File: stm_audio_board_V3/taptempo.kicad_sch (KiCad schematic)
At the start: 2 parts

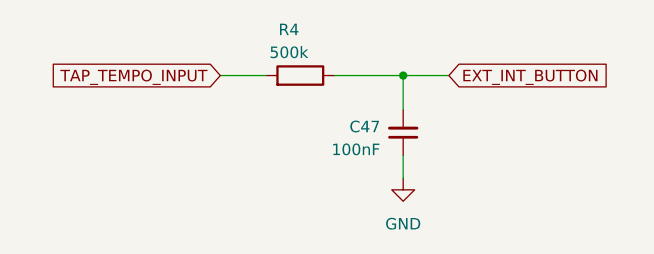
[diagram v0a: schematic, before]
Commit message: Input and output stages are made and assembly started on pcb view
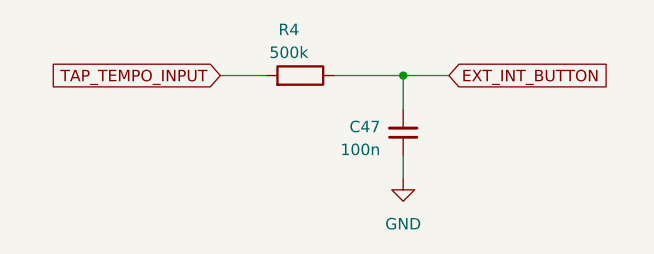
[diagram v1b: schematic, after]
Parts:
- C47: value 100nF -> 100n; footprint Capacitor_SMD:C_0603_1608Metric_Pad1.08x0.95mm_HandSolder -> Capacitor_SMD:C_0603_1608Metric
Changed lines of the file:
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@@
       (effects (font (size 1.27 1.27)) (justify right))
     )
-    (property "Value" "100nF" (at 54.61 53.9686 0)
+    (property "Value" "100n" (at 54.61 53.9686 0)
       (effects (font (size 1.27 1.27)) (justify right))
     )
-    (property "Footprint" "Capacitor_SMD:C_0603_1608Metric_Pad1.08x0.95mm_HandSolder" (at 57.15 52.07 0)
+    (property "Footprint" "Capacitor_SMD:C_0603_1608Metric" (at 57.15 52.07 0)
       (effects (font (size 1.27 1.27)) hide)
     )

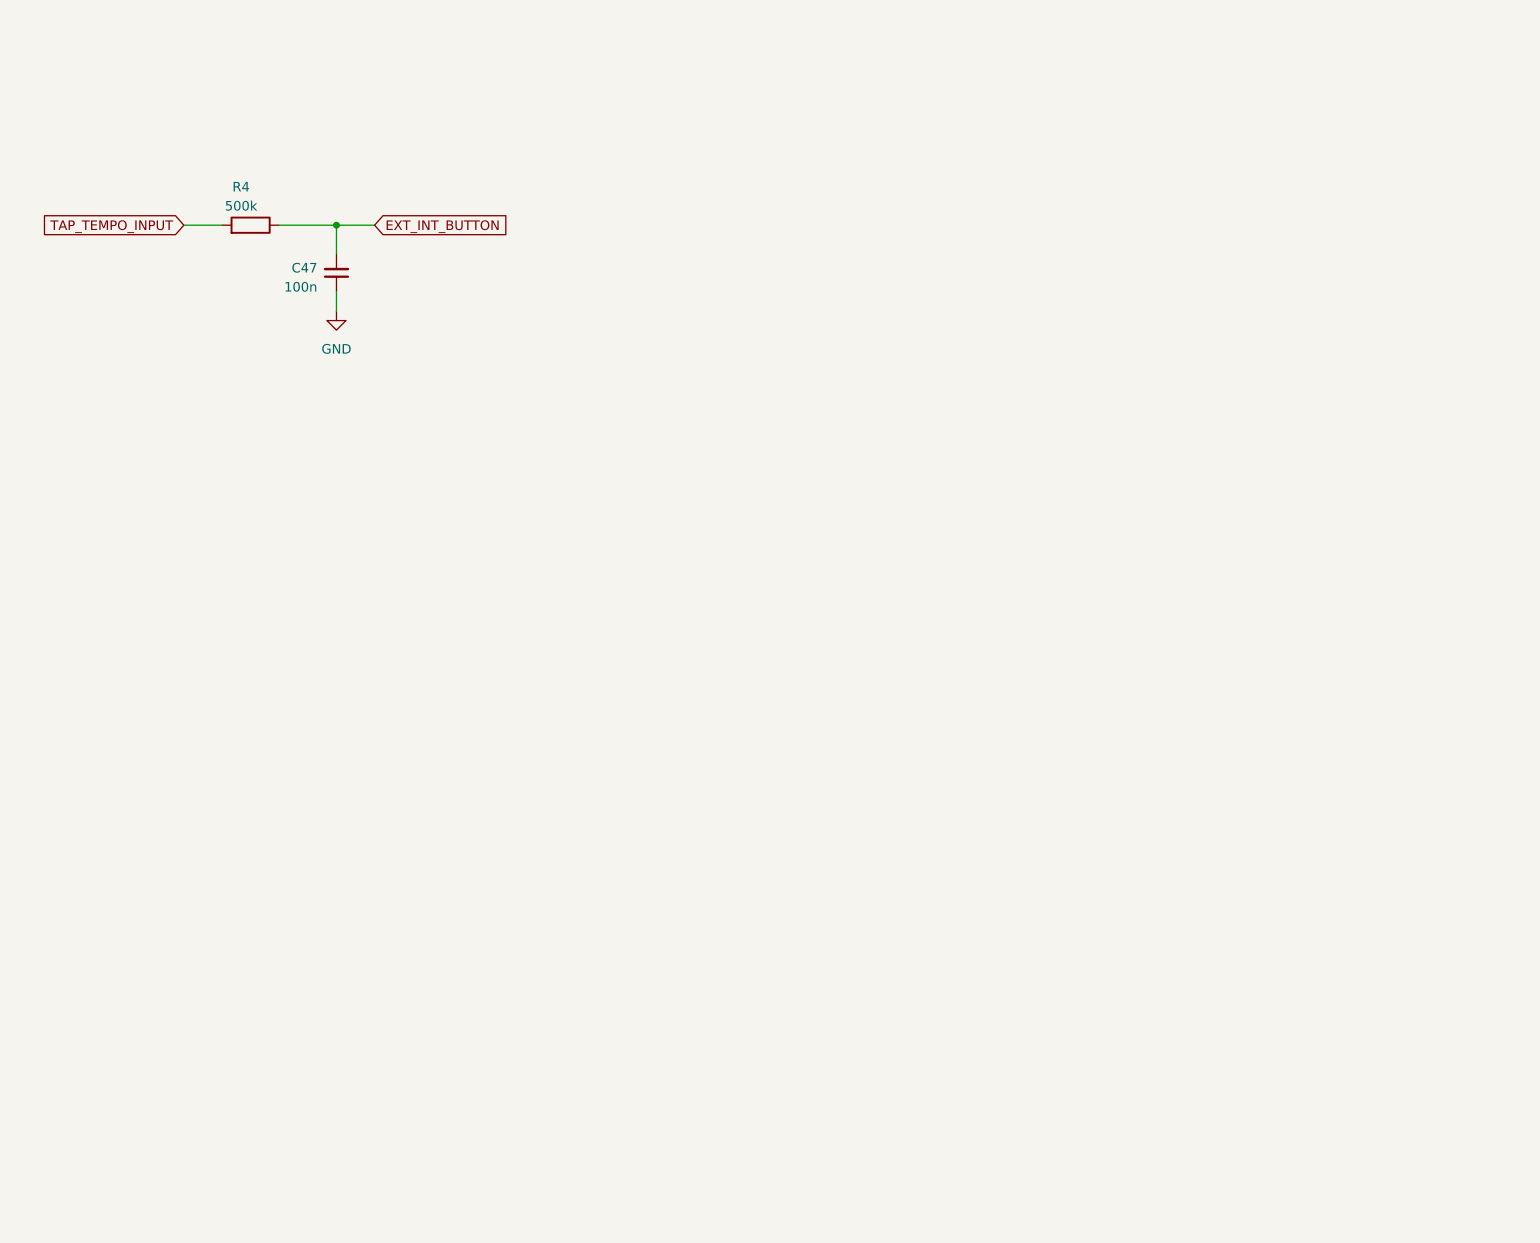
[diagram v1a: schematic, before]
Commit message: Footswitch debounce added
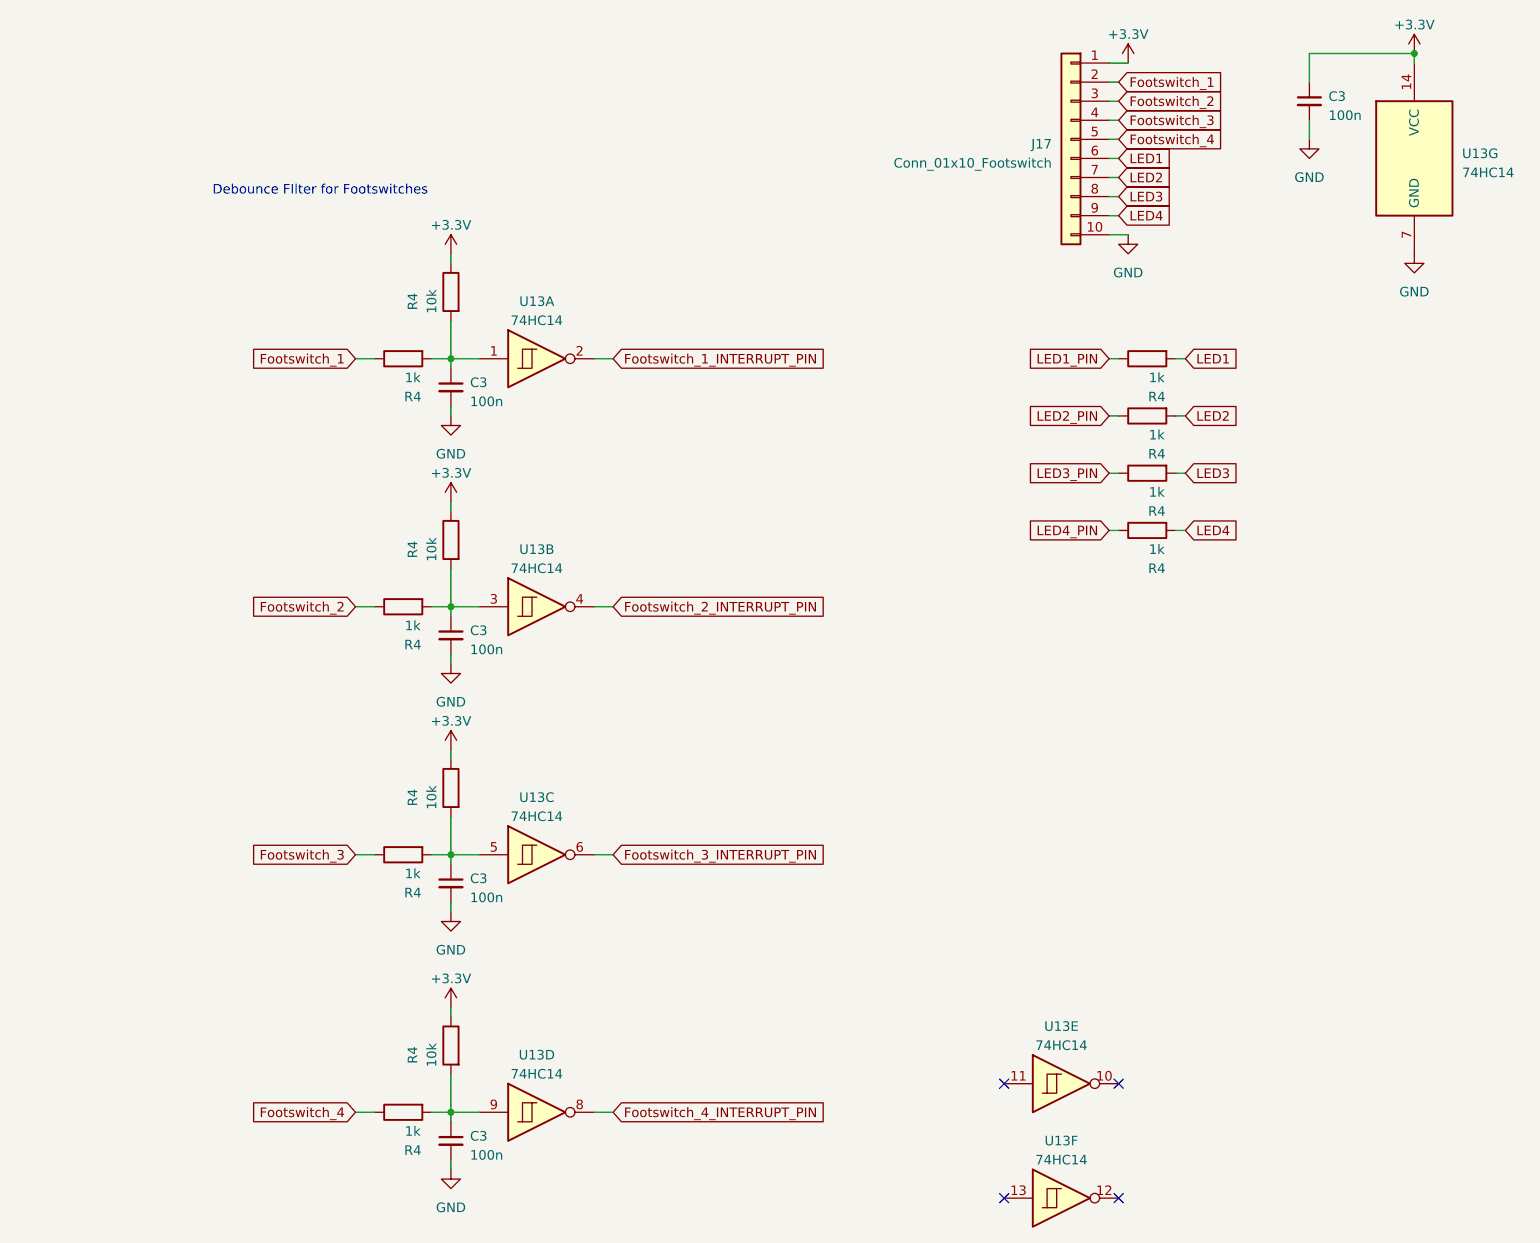
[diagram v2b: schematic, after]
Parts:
- removed C47: 100n, Capacitor_SMD:C_0603_1608Metric, symbol Device:C_Small
- removed R4: 500k, Resistor_SMD:R_0805_2012Metric_Pad1.20x1.40mm_HandSolder, symbol Device:R
- added C3 (x5): 100n, Capacitor_SMD:C_0603_1608Metric, symbol Device:C_Small
- added J17: Conn_01x10_Footswitch, Connector_IDC:IDC-Header_2x05_P2.54mm_Vertical, symbol Connector_Generic:Conn_01x10
- added R4 (x8): 1k, Resistor_SMD:R_0603_1608Metric_Pad0.98x0.95mm_HandSolder, symbol Device:R
- added R4 (x4): 10k, Resistor_SMD:R_0603_1608Metric_Pad0.98x0.95mm_HandSolder, symbol Device:R
- added U13: 74HC14, Package_SO:SOIC-14_3.9x8.7mm_P1.27mm, symbol 74xx:74HC14
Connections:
- net GND: now also C3.2, C3.2, C3.2, C3.2, C3.2, J17.10 (Pin_10), U13.7 (GND)
- new net: C3.1, R4.2, R4.2, U13.1
- new net: C3.1, R4.2, R4.2, U13.5
- new net: C3.1, R4.2, R4.2, U13.3
- new net: C3.1, R4.2, R4.2, U13.9
- new net +3.3V: C3.1, J17.1 (Pin_1), R4.1, R4.1, R4.1, R4.1, U13.14 (VCC)
- new net Footswitch_1: J17.2 (Pin_2), R4.1
- new net Footswitch_1_INTERRUPT_PIN: U13.2
- new net Footswitch_2: J17.3 (Pin_3), R4.1
- new net Footswitch_2_INTERRUPT_PIN: U13.4
- new net Footswitch_3: J17.4 (Pin_4), R4.1
- new net Footswitch_3_INTERRUPT_PIN: U13.6
- new net Footswitch_4: J17.5 (Pin_5), R4.1
- new net Footswitch_4_INTERRUPT_PIN: U13.8
- new net LED1: J17.6 (Pin_6), R4.2
- new net LED1_PIN: R4.1
- new net LED2: J17.7 (Pin_7), R4.2
- new net LED2_PIN: R4.1
- new net LED3: J17.8 (Pin_8), R4.2
- new net LED3_PIN: R4.1
- new net LED4: J17.9 (Pin_9), R4.2
- new net LED4_PIN: R4.1
- no-connect marks 0 -> 4
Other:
- note added: "Debounce FIlter for Footswitches"

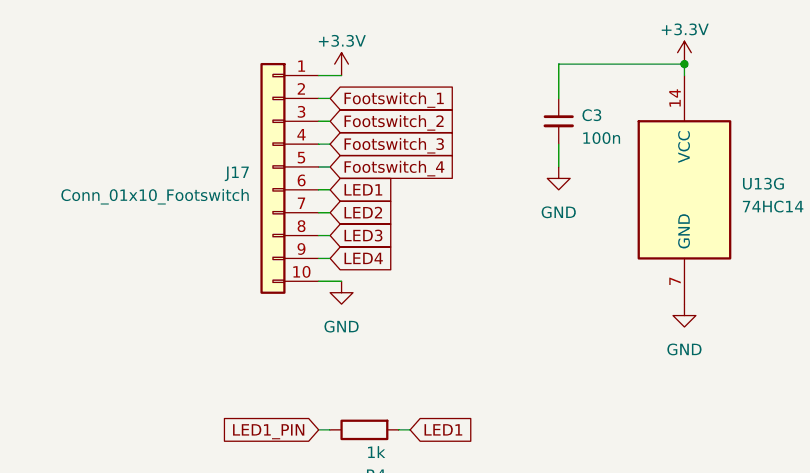
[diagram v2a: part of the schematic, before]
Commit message: gnd vias added, footswitch mux connected
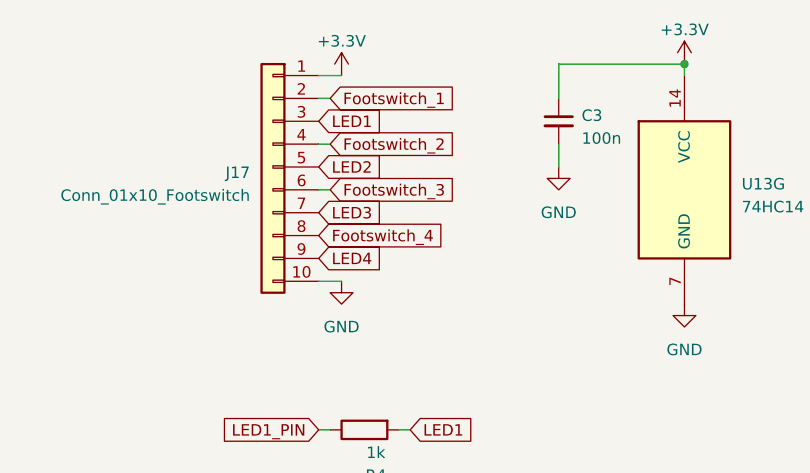
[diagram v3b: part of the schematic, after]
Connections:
- net Footswitch_2: now also J17.4 (Pin_4); no longer J17.3 (Pin_3)
- net Footswitch_3: now also J17.6 (Pin_6); no longer J17.4 (Pin_4)
- net Footswitch_4: now also J17.8 (Pin_8); no longer J17.5 (Pin_5)
- net LED1: now also J17.3 (Pin_3); no longer J17.6 (Pin_6)
- net LED2: now also J17.5 (Pin_5); no longer J17.7 (Pin_7)
- net LED3: now also J17.7 (Pin_7); no longer J17.8 (Pin_8)
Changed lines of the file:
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@@
-    (stroke (width 0) (type default))
-  )
-  (wire (pts (xy 160.02 41.91) (xy 161.29 41.91))
     (stroke (width 0) (type default))
   )
@@
     (stroke (width 0) (type default))
   )
+  (wire (pts (xy 161.29 36.83) (xy 160.02 36.83))
+    (stroke (width 0) (type default))
+  )
   (wire (pts (xy 72.39 129.54) (xy 72.39 130.81))
     (stroke (width 0) (type default))
   )
-  (wire (pts (xy 160.02 39.37) (xy 161.29 39.37))
-    (stroke (width 0) (type default))
-  )
-  (wire (pts (xy 160.02 44.45) (xy 161.29 44.45))
-    (stroke (width 0) (type default))
-  )
-  (wire (pts (xy 160.02 36.83) (xy 161.29 36.83))
-    (stroke (width 0) (type default))
-  )
   (wire (pts (xy 160.02 71.12) (xy 161.29 71.12))
     (stroke (width 0) (type default))
@@
     (stroke (width 0) (type default))
   )
-  (wire (pts (xy 160.02 29.21) (xy 161.29 29.21))
-    (stroke (width 0) (type default))
-  )
   (wire (pts (xy 59.69 129.54) (xy 62.23 129.54))
     (stroke (width 0) (type default))
@@
     (stroke (width 0) (type default))
   )
-  (wire (pts (xy 160.02 31.75) (xy 161.29 31.75))
-    (stroke (width 0) (type default))
-  )
   (wire (pts (xy 168.91 78.74) (xy 170.18 78.74))
     (stroke (width 0) (type default))
   )
-  (wire (pts (xy 160.02 34.29) (xy 161.29 34.29))
-    (stroke (width 0) (type default))
-  )
   (wire (pts (xy 160.02 63.5) (xy 161.29 63.5))
     (stroke (width 0) (type default))
@@
   )
   (wire (pts (xy 72.39 82.55) (xy 72.39 83.82))
+    (stroke (width 0) (type default))
+  )
+  (wire (pts (xy 161.29 31.75) (xy 160.02 31.75))
     (stroke (width 0) (type default))
   )
@@
     (effects (font (size 1.27 1.27)) (justify left bottom))
   )
-  (global_label "LED3" (shape input) (at 161.29 41.91 0) (fields_autoplaced)
-    (effects (font (size 1.27 1.27)) (justify left))
-    (property "Intersheetrefs" "${INTERSHEET_REFS}" (at 168.8524 41.91 0)
+  (global_label "LED3" (shape input) (at 160.02 39.37 0) (fields_autoplaced)
+    (effects (font (size 1.27 1.27)) (justify left))
+    (property "Intersheetrefs" "${INTERSHEET_REFS}" (at 167.5824 39.37 0)
       (effects (font (size 1.27 1.27)) (justify left) hide)
     )
@@
     )
   )
-  (global_label "LED1" (shape input) (at 161.29 36.83 0) (fields_autoplaced)
-    (effects (font (size 1.27 1.27)) (justify left))
-    (property "Intersheetrefs" "${INTERSHEET_REFS}" (at 168.8524 36.83 0)
+  (global_label "LED1" (shape input) (at 160.02 29.21 0) (fields_autoplaced)
+    (effects (font (size 1.27 1.27)) (justify left))
+    (property "Intersheetrefs" "${INTERSHEET_REFS}" (at 167.5824 29.21 0)
       (effects (font (size 1.27 1.27)) (justify left) hide)
     )
@@
     )
   )
-  (global_label "Footswitch_4" (shape input) (at 161.29 34.29 0) (fields_autoplaced)
-    (effects (font (size 1.27 1.27)) (justify left))
-    (property "Intersheetrefs" "${INTERSHEET_REFS}" (at 176.4119 34.29 0)
+  (global_label "Footswitch_4" (shape input) (at 160.02 41.91 0) (fields_autoplaced)
+    (effects (font (size 1.27 1.27)) (justify left))
+    (property "Intersheetrefs" "${INTERSHEET_REFS}" (at 175.1419 41.91 0)
       (effects (font (size 1.27 1.27)) (justify left) hide)
     )
@@
     )
   )
-  (global_label "Footswitch_3" (shape input) (at 161.29 31.75 0) (fields_autoplaced)
+  (global_label "Footswitch_3" (shape input) (at 161.29 36.83 0) (fields_autoplaced)
+    (effects (font (size 1.27 1.27)) (justify left))
+    (property "Intersheetrefs" "${INTERSHEET_REFS}" (at 176.4119 36.83 0)
+      (effects (font (size 1.27 1.27)) (justify left) hide)
+    )
+  )
+  (global_label "LED3_PIN" (shape input) (at 160.02 78.74 180) (fields_autoplaced)
+    (effects (font (size 1.27 1.27)) (justify right))
+    (property "Intersheetrefs" "${INTERSHEET_REFS}" (at 148.2847 78.74 0)
+      (effects (font (size 1.27 1.27)) (justify right) hide)
+    )
+  )
+  (global_label "Footswitch_2_INTERRUPT_PIN" (shape input) (at 93.98 96.52 0) (fields_autoplaced)
+    (effects (font (size 1.27 1.27)) (justify left))
+    (property "Intersheetrefs" "${INTERSHEET_REFS}" (at 124.4024 96.52 0)
+      (effects (font (size 1.27 1.27)) (justify left) hide)
+    )
+  )
+  (global_label "Footswitch_2" (shape input) (at 59.69 96.52 180) (fields_autoplaced)
+    (effects (font (size 1.27 1.27)) (justify right))
+    (property "Intersheetrefs" "${INTERSHEET_REFS}" (at 44.5681 96.52 0)
+      (effects (font (size 1.27 1.27)) (justify right) hide)
+    )
+  )
+  (global_label "LED4" (shape input) (at 160.02 44.45 0) (fields_autoplaced)
+    (effects (font (size 1.27 1.27)) (justify left))
+    (property "Intersheetrefs" "${INTERSHEET_REFS}" (at 167.5824 44.45 0)
+      (effects (font (size 1.27 1.27)) (justify left) hide)
+    )
+  )
+  (global_label "LED2" (shape input) (at 160.02 34.29 0) (fields_autoplaced)
+    (effects (font (size 1.27 1.27)) (justify left))
+    (property "Intersheetrefs" "${INTERSHEET_REFS}" (at 167.5824 34.29 0)
+      (effects (font (size 1.27 1.27)) (justify left) hide)
+    )
+  )
+  (global_label "LED2_PIN" (shape input) (at 160.02 71.12 180) (fields_autoplaced)
+    (effects (font (size 1.27 1.27)) (justify right))
+    (property "Intersheetrefs" "${INTERSHEET_REFS}" (at 148.2847 71.12 0)
+      (effects (font (size 1.27 1.27)) (justify right) hide)
+    )
+  )
+  (global_label "LED1" (shape input) (at 170.18 63.5 0) (fields_autoplaced)
+    (effects (font (size 1.27 1.27)) (justify left))
+    (property "Intersheetrefs" "${INTERSHEET_REFS}" (at 177.7424 63.5 0)
+      (effects (font (size 1.27 1.27)) (justify left) hide)
+    )
+  )
+  (global_label "Footswitch_4" (shape input) (at 59.69 163.83 180) (fields_autoplaced)
+    (effects (font (size 1.27 1.27)) (justify right))
+    (property "Intersheetrefs" "${INTERSHEET_REFS}" (at 44.5681 163.83 0)
+      (effects (font (size 1.27 1.27)) (justify right) hide)
+    )
+  )
+  (global_label "Footswitch_1" (shape input) (at 59.69 63.5 180) (fields_autoplaced)
+    (effects (font (size 1.27 1.27)) (justify right))
+    (property "Intersheetrefs" "${INTERSHEET_REFS}" (at 44.5681 63.5 0)
+      (effects (font (size 1.27 1.27)) (justify right) hide)
+    )
+  )
+  (global_label "LED1_PIN" (shape input) (at 160.02 63.5 180) (fields_autoplaced)
+    (effects (font (size 1.27 1.27)) (justify right))
+    (property "Intersheetrefs" "${INTERSHEET_REFS}" (at 148.2847 63.5 0)
+      (effects (font (size 1.27 1.27)) (justify right) hide)
+    )
+  )
+  (global_label "Footswitch_2" (shape input) (at 161.29 31.75 0) (fields_autoplaced)
     (effects (font (size 1.27 1.27)) (justify left))
     (property "Intersheetrefs" "${INTERSHEET_REFS}" (at 176.4119 31.75 0)
       (effects (font (size 1.27 1.27)) (justify left) hide)
     )
-  )
-  (global_label "LED3_PIN" (shape input) (at 160.02 78.74 180) (fields_autoplaced)
-    (effects (font (size 1.27 1.27)) (justify right))
-    (property "Intersheetrefs" "${INTERSHEET_REFS}" (at 148.2847 78.74 0)
-      (effects (font (size 1.27 1.27)) (justify right) hide)
-    )
-  )
-  (global_label "Footswitch_2_INTERRUPT_PIN" (shape input) (at 93.98 96.52 0) (fields_autoplaced)
-    (effects (font (size 1.27 1.27)) (justify left))
-    (property "Intersheetrefs" "${INTERSHEET_REFS}" (at 124.4024 96.52 0)
-      (effects (font (size 1.27 1.27)) (justify left) hide)
-    )
-  )
-  (global_label "Footswitch_2" (shape input) (at 59.69 96.52 180) (fields_autoplaced)
-    (effects (font (size 1.27 1.27)) (justify right))
-    (property "Intersheetrefs" "${INTERSHEET_REFS}" (at 44.5681 96.52 0)
-      (effects (font (size 1.27 1.27)) (justify right) hide)
-    )
-  )
-  (global_label "LED4" (shape input) (at 161.29 44.45 0) (fields_autoplaced)
-    (effects (font (size 1.27 1.27)) (justify left))
-    (property "Intersheetrefs" "${INTERSHEET_REFS}" (at 168.8524 44.45 0)
-      (effects (font (size 1.27 1.27)) (justify left) hide)
-    )
-  )
-  (global_label "LED2" (shape input) (at 161.29 39.37 0) (fields_autoplaced)
-    (effects (font (size 1.27 1.27)) (justify left))
-    (property "Intersheetrefs" "${INTERSHEET_REFS}" (at 168.8524 39.37 0)
-      (effects (font (size 1.27 1.27)) (justify left) hide)
-    )
-  )
-  (global_label "LED2_PIN" (shape input) (at 160.02 71.12 180) (fields_autoplaced)
-    (effects (font (size 1.27 1.27)) (justify right))
-    (property "Intersheetrefs" "${INTERSHEET_REFS}" (at 148.2847 71.12 0)
-      (effects (font (size 1.27 1.27)) (justify right) hide)
-    )
-  )
-  (global_label "LED1" (shape input) (at 170.18 63.5 0) (fields_autoplaced)
-    (effects (font (size 1.27 1.27)) (justify left))
-    (property "Intersheetrefs" "${INTERSHEET_REFS}" (at 177.7424 63.5 0)
-      (effects (font (size 1.27 1.27)) (justify left) hide)
-    )
-  )
-  (global_label "Footswitch_4" (shape input) (at 59.69 163.83 180) (fields_autoplaced)
-    (effects (font (size 1.27 1.27)) (justify right))
-    (property "Intersheetrefs" "${INTERSHEET_REFS}" (at 44.5681 163.83 0)
-      (effects (font (size 1.27 1.27)) (justify right) hide)
-    )
-  )
-  (global_label "Footswitch_1" (shape input) (at 59.69 63.5 180) (fields_autoplaced)
-    (effects (font (size 1.27 1.27)) (justify right))
-    (property "Intersheetrefs" "${INTERSHEET_REFS}" (at 44.5681 63.5 0)
-      (effects (font (size 1.27 1.27)) (justify right) hide)
-    )
-  )
-  (global_label "LED1_PIN" (shape input) (at 160.02 63.5 180) (fields_autoplaced)
-    (effects (font (size 1.27 1.27)) (justify right))
-    (property "Intersheetrefs" "${INTERSHEET_REFS}" (at 148.2847 63.5 0)
-      (effects (font (size 1.27 1.27)) (justify right) hide)
-    )
-  )
-  (global_label "Footswitch_2" (shape input) (at 161.29 29.21 0) (fields_autoplaced)
-    (effects (font (size 1.27 1.27)) (justify left))
-    (property "Intersheetrefs" "${INTERSHEET_REFS}" (at 176.4119 29.21 0)
-      (effects (font (size 1.27 1.27)) (justify left) hide)
-    )
